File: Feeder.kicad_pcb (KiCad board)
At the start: 2 copper layers, 20 x 11 mm, 13 parts, among them J1 UPDI, J2 Internal, J3 RS485, Q1 2N7002NXAKR, U1 ATtiny402, U2 ST485EBDR

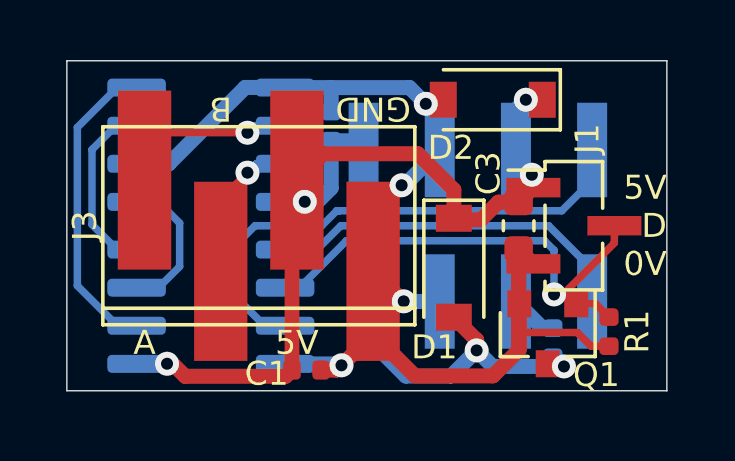
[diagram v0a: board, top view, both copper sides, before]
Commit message: Invert Motor and Feedback: Allow to use UPDI pin always as input and may avoid damaged IC
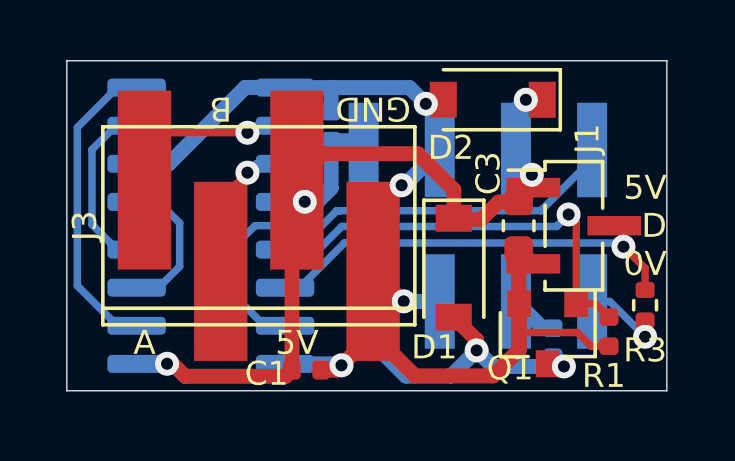
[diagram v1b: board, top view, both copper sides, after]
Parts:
- added R3: 1k, Resistor_SMD:R_0402_1005Metric, F.Cu at (99.3, 68.2)
- R2: value 0 -> NP
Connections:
- J1 pad 2: /UPDI -> /FEEDBACK
- J2 pad 8: /FEEDBACK -> Net-(J2-Pad8)
- Q1 pad 1: /UPDI -> /MOTOR
- R1 pad 1: /UPDI -> /MOTOR
- U1 pad 5: /FEEDBACK -> /MOTOR
- U1 pad 6: /UPDI -> /FEEDBACK
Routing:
- net /UPDI: track 17.3 -> 0.00 mm, vias 1 -> 0
- net /MOTOR: track 0.00 -> 14.3 mm, vias 0 -> 1
- net Net-(J2-Pad8): track 0.00 -> 3.07 mm, vias 0 -> 1
- net /FEEDBACK: track 12.5 -> 14.9 mm, vias 0 -> 1
